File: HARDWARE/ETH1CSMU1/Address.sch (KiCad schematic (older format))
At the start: 16 parts, among them U1501 STEF4S

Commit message: check in
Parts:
- C1501, C1502: footprint (none) -> SMD:C_0603_Symbol1
- R1501, R1502, R1503, R1504: footprint (none) -> SMD:R_0603_Symbol10
- U1501: footprint (none) -> Housings_DFN_QFN:DFN-10-1EP_3x3mm_Pitch0.5mm
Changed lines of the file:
@@
 F 0 "R1501" V 5843 3250 50  0000 C CNN
 F 1 "100" V 5934 3250 50  0000 C CNN
-F 2 "" V 5980 3250 50  0001 C CNN
+F 2 "SMD:R_0603_Symbol10" V 5980 3250 50  0001 C CNN
 F 3 "~" H 6050 3250 50  0001 C CNN
 	1    6050 3250
@@
 F 0 "R1502" V 5843 4050 50  0000 C CNN
 F 1 "100" V 5934 4050 50  0000 C CNN
-F 2 "" V 5980 4050 50  0001 C CNN
+F 2 "SMD:R_0603_Symbol10" V 5980 4050 50  0001 C CNN
 F 3 "~" H 6050 4050 50  0001 C CNN
 	1    6050 4050
@@
 F 0 "R1503" V 5843 4850 50  0000 C CNN
 F 1 "100" V 5934 4850 50  0000 C CNN
-F 2 "" V 5980 4850 50  0001 C CNN
+F 2 "SMD:R_0603_Symbol10" V 5980 4850 50  0001 C CNN
 F 3 "~" H 6050 4850 50  0001 C CNN
 	1    6050 4850
@@
 F 0 "R1504" V 5843 5650 50  0000 C CNN
 F 1 "100" V 5934 5650 50  0000 C CNN
-F 2 "" V 5980 5650 50  0001 C CNN
+F 2 "SMD:R_0603_Symbol10" V 5980 5650 50  0001 C CNN
 F 3 "~" H 6050 5650 50  0001 C CNN
 	1    6050 5650
@@
 F 0 "U1501" H 5550 2565 50  0000 C CNN
 F 1 "STEF4S" H 5550 2474 50  0000 C CNN
-F 2 "" H 5650 2500 50  0001 C CNN
+F 2 "Housings_DFN_QFN:DFN-10-1EP_3x3mm_Pitch0.5mm" H 5650 2500 50  0001 C CNN
 F 3 "" H 5650 2500 50  0001 C CNN
 	1    5550 2000
@@
 F 0 "C1501" H 4915 2546 50  0000 L CNN
 F 1 "100n" H 4915 2455 50  0000 L CNN
-F 2 "" H 4838 2350 50  0001 C CNN
+F 2 "SMD:C_0603_Symbol1" H 4838 2350 50  0001 C CNN
 F 3 "~" H 4800 2500 50  0001 C CNN
 	1    4800 2500
@@
 F 0 "C1502" H 6365 1946 50  0000 L CNN
 F 1 "100n" H 6365 1855 50  0000 L CNN
-F 2 "" H 6288 1750 50  0001 C CNN
+F 2 "SMD:C_0603_Symbol1" H 6288 1750 50  0001 C CNN
 F 3 "~" H 6250 1900 50  0001 C CNN
 	1    6250 1900

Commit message: Check in
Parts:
- C1503: footprint (none) -> SMD:C_0603_Symbol6
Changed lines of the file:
@@
 F 0 "C1503" H 6815 1946 50  0000 L CNN
 F 1 "1u" H 6815 1855 50  0000 L CNN
-F 2 "" H 6738 1750 50  0001 C CNN
+F 2 "SMD:C_0603_Symbol6" H 6738 1750 50  0001 C CNN
 F 3 "~" H 6700 1900 50  0001 C CNN
 	1    6700 1900

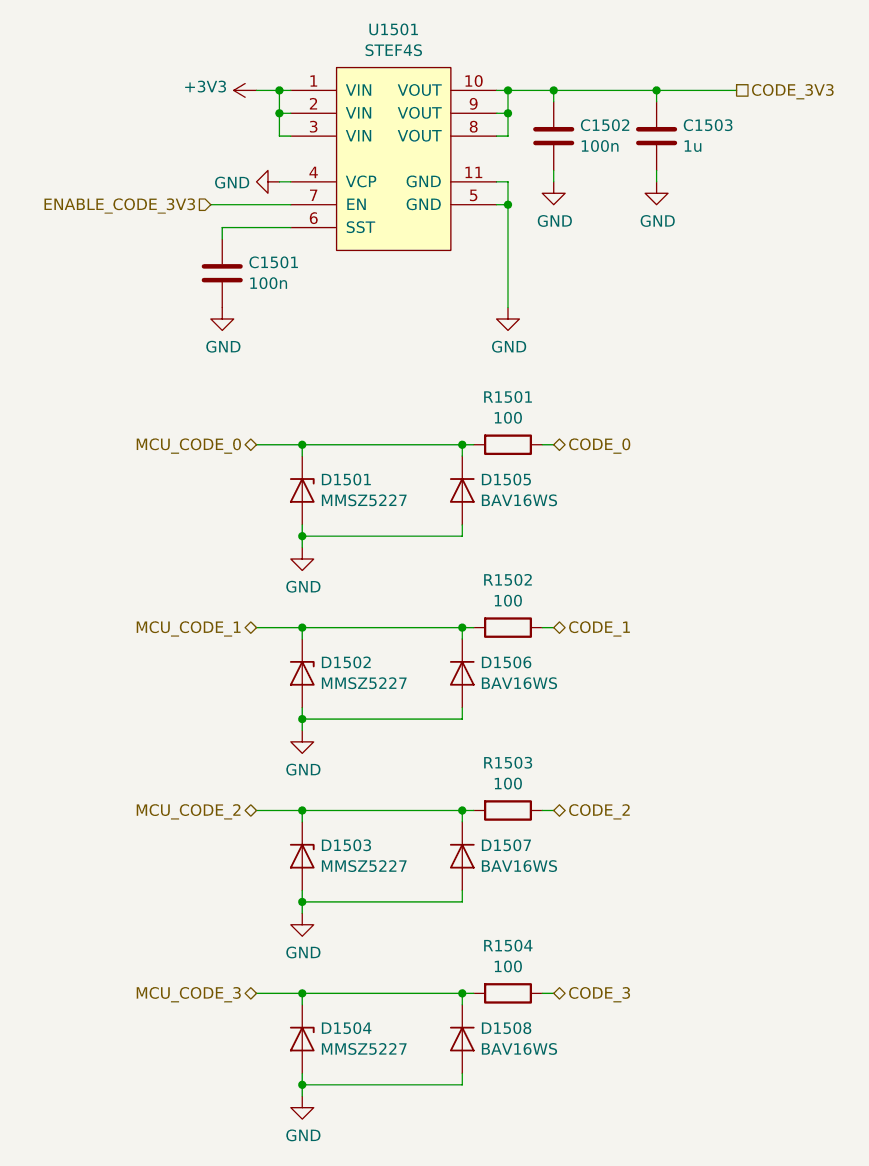
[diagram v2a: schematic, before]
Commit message: Added test circuits, bug fix.
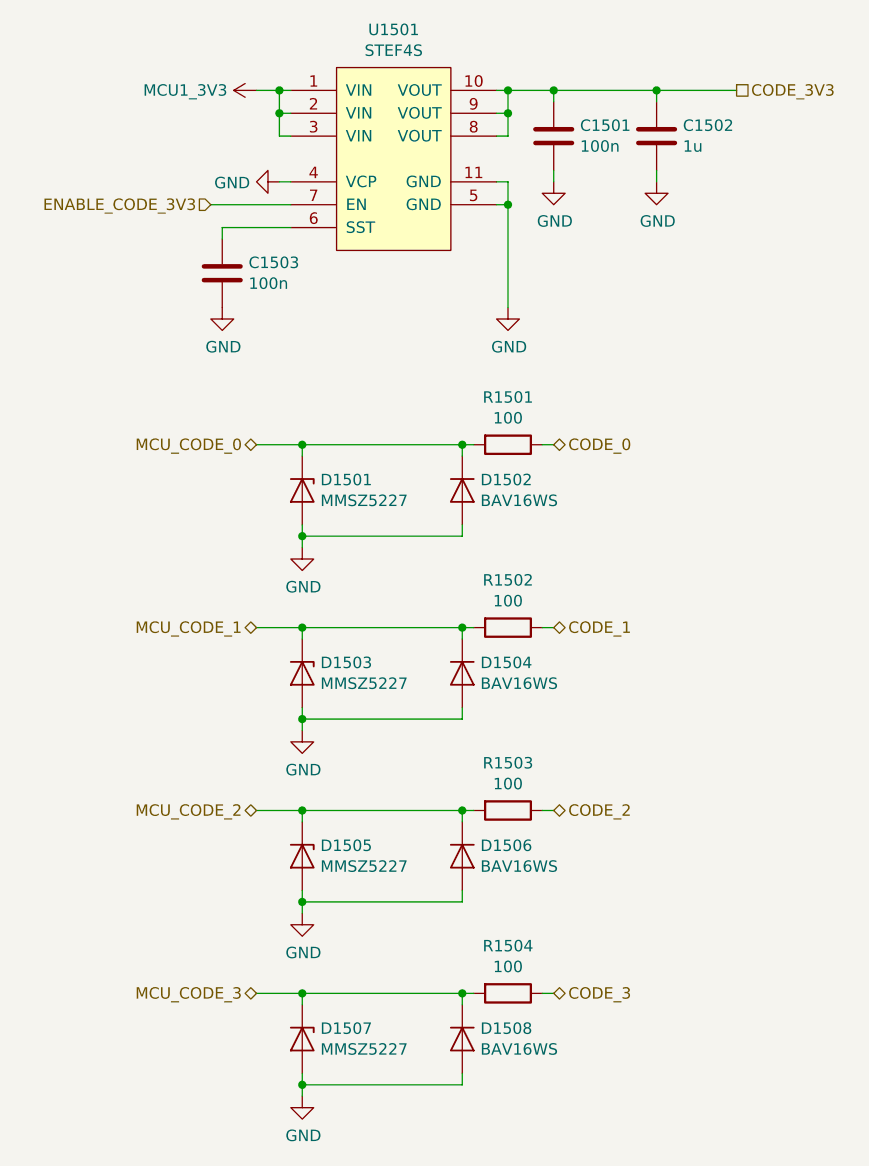
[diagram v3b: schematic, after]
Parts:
- renumbered C1502 to C1501, C1503 to C1502, C1501 to C1503, D1505 to D1502, D1502 to D1503, D1506 to D1504, D1503 to D1505, D1507 to D1506, D1504 to D1507
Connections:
- net +3V3 renamed MCU1_3V3
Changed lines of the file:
@@
 $Descr A4 11693 8268
 encoding utf-8
-Sheet 15 15
+Sheet 15 16
 Title ""
 Date ""
@@
 $EndComp
 $Comp
-L Device:D D1505
+L Device:D D1502
 U 1 1 5C0E460B
 P 5850 3450
-F 0 "D1505" V 5804 3529 50  0000 L CNN
+F 0 "D1502" V 5804 3529 50  0000 L CNN
 F 1 "BAV16WS" V 5895 3529 50  0000 L CNN
 F 2 "Diodes_SMD:D_SOD-323_HandSoldering" H 5850 3450 50  0001 C CNN
@@
 	5850 3650 5850 3600
 $Comp
-L power:GND #PWR01504
+L power:GND #PWR01507
 U 1 1 5C0E4AA9
 P 5150 3700
-F 0 "#PWR01504" H 5150 3450 50  0001 C CNN
+F 0 "#PWR01507" H 5150 3450 50  0001 C CNN
 F 1 "GND" H 5155 3527 50  0000 C CNN
 F 2 "" H 5150 3700 50  0001 C CNN
@@
 CODE_3V3
 $Comp
-L power:+3V3 #PWR01502
-U 1 1 5C0E762F
-P 4950 1700
-F 0 "#PWR01502" H 4950 1550 50  0001 C CNN
-F 1 "+3V3" V 4965 1828 50  0000 L CNN
-F 2 "" H 4950 1700 50  0001 C CNN
-F 3 "" H 4950 1700 50  0001 C CNN
-	1    4950 1700
-	0    -1   -1   0
-$EndComp
-$Comp
-L Device:D D1506
+L Device:D D1504
 U 1 1 5C12B8C6
 P 5850 4250
-F 0 "D1506" V 5804 4329 50  0000 L CNN
+F 0 "D1504" V 5804 4329 50  0000 L CNN
 F 1 "BAV16WS" V 5895 4329 50  0000 L CNN
 F 2 "Diodes_SMD:D_SOD-323_HandSoldering" H 5850 4250 50  0001 C CNN
@@
 	5850 4050 5900 4050
 $Comp
-L Device:D_Zener D1502
+L Device:D_Zener D1503
 U 1 1 5C12B8CF
 P 5150 4250
-F 0 "D1502" V 5104 4329 50  0000 L CNN
+F 0 "D1503" V 5104 4329 50  0000 L CNN
 F 1 "MMSZ5227" V 5195 4329 50  0000 L CNN
 F 2 "Diodes_SMD:D_SOD-123" H 5150 4250 50  0001 C CNN
@@
 	5850 4450 5850 4400
 $Comp
-L power:GND #PWR01505
+L power:GND #PWR01508
 U 1 1 5C12B8DC
 P 5150 4500
-F 0 "#PWR01505" H 5150 4250 50  0001 C CNN
+F 0 "#PWR01508" H 5150 4250 50  0001 C CNN
 F 1 "GND" H 5155 4327 50  0000 C CNN
 F 2 "" H 5150 4500 50  0001 C CNN
@@
 Connection ~ 5150 4050
 $Comp
-L Device:D D1507
+L Device:D D1506
 U 1 1 5C12C933
 P 5850 5050
-F 0 "D1507" V 5804 5129 50  0000 L CNN
+F 0 "D1506" V 5804 5129 50  0000 L CNN
 F 1 "BAV16WS" V 5895 5129 50  0000 L CNN
 F 2 "Diodes_SMD:D_SOD-323_HandSoldering" H 5850 5050 50  0001 C CNN
@@
 	5850 4850 5900 4850
 $Comp
-L Device:D_Zener D1503
+L Device:D_Zener D1505
 U 1 1 5C12C93B
 P 5150 5050
-F 0 "D1503" V 5104 5129 50  0000 L CNN
+F 0 "D1505" V 5104 5129 50  0000 L CNN
 F 1 "MMSZ5227" V 5195 5129 50  0000 L CNN
 F 2 "Diodes_SMD:D_SOD-123" H 5150 5050 50  0001 C CNN
@@
 	5850 5250 5850 5200
 $Comp
-L power:GND #PWR01506
+L power:GND #PWR01509
 U 1 1 5C12C947
 P 5150 5300
-F 0 "#PWR01506" H 5150 5050 50  0001 C CNN
+F 0 "#PWR01509" H 5150 5050 50  0001 C CNN
 F 1 "GND" H 5155 5127 50  0000 C CNN
 F 2 "" H 5150 5300 50  0001 C CNN
@@
 	5850 5650 5900 5650
 $Comp
-L Device:D_Zener D1504
+L Device:D_Zener D1507
 U 1 1 5C12C959
 P 5150 5850
-F 0 "D1504" V 5104 5929 50  0000 L CNN
+F 0 "D1507" V 5104 5929 50  0000 L CNN
 F 1 "MMSZ5227" V 5195 5929 50  0000 L CNN
 F 2 "Diodes_SMD:D_SOD-123" H 5150 5850 50  0001 C CNN
@@
 	5850 6050 5850 6000
 $Comp
-L power:GND #PWR01507
+L power:GND #PWR01510
 U 1 1 5C12C965
 P 5150 6100
-F 0 "#PWR01507" H 5150 5850 50  0001 C CNN
+F 0 "#PWR01510" H 5150 5850 50  0001 C CNN
 F 1 "GND" H 5155 5927 50  0000 C CNN
 F 2 "" H 5150 6100 50  0001 C CNN
@@
 Connection ~ 5050 1700
 $Comp
-L power:GND #PWR01508
+L power:GND #PWR01506
 U 1 1 5C0DDDA0
 P 6050 2650
-F 0 "#PWR01508" H 6050 2400 50  0001 C CNN
+F 0 "#PWR01506" H 6050 2400 50  0001 C CNN
 F 1 "GND" H 6055 2477 50  0000 C CNN
 F 2 "" H 6050 2650 50  0001 C CNN
@@
 	5100 2200 4750 2200
 $Comp
-L power:GND #PWR01503
+L power:GND #PWR01502
 U 1 1 5C0E284A
 P 5050 2100
-F 0 "#PWR01503" H 5050 1850 50  0001 C CNN
+F 0 "#PWR01502" H 5050 1850 50  0001 C CNN
 F 1 "GND" V 5055 1972 50  0000 R CNN
 F 2 "" H 5050 2100 50  0001 C CNN
@@
 	5050 2100 5100 2100
 $Comp
-L Device:C C1501
+L Device:C C1503
 U 1 1 5C0E6BCC
 P 4800 2500
-F 0 "C1501" H 4915 2546 50  0000 L CNN
+F 0 "C1503" H 4915 2546 50  0000 L CNN
 F 1 "100n" H 4915 2455 50  0000 L CNN
 F 2 "SMD:C_0603_Symbol1" H 4838 2350 50  0001 C CNN
@@
 	4800 2300 4800 2350
 $Comp
-L power:GND #PWR01501
+L power:GND #PWR01505
 U 1 1 5C0E8A75
 P 4800 2650
-F 0 "#PWR01501" H 4800 2400 50  0001 C CNN
+F 0 "#PWR01505" H 4800 2400 50  0001 C CNN
 F 1 "GND" H 4805 2477 50  0000 C CNN
 F 2 "" H 4800 2650 50  0001 C CNN
@@
 ENABLE_CODE_3V3
 $Comp
-L Device:C C1502
+L Device:C C1501
 U 1 1 5C0EFAE2
 P 6250 1900
-F 0 "C1502" H 6365 1946 50  0000 L CNN
+F 0 "C1501" H 6365 1946 50  0000 L CNN
 F 1 "100n" H 6365 1855 50  0000 L CNN
 F 2 "SMD:C_0603_Symbol1" H 6288 1750 50  0001 C CNN
@@
 $EndComp
 $Comp
-L Device:C C1503
+L Device:C C1502
 U 1 1 5C0F2F4D
 P 6700 1900
-F 0 "C1503" H 6815 1946 50  0000 L CNN
+F 0 "C1502" H 6815 1946 50  0000 L CNN
 F 1 "1u" H 6815 1855 50  0000 L CNN
 F 2 "SMD:C_0603_Symbol6" H 6738 1750 50  0001 C CNN
@@
 	6700 1700 6250 1700
 $Comp
-L power:GND #PWR01509
+L power:GND #PWR01503
 U 1 1 5C0F750B
 P 6250 2100
-F 0 "#PWR01509" H 6250 1850 50  0001 C CNN
+F 0 "#PWR01503" H 6250 1850 50  0001 C CNN
 F 1 "GND" H 6255 1927 50  0000 C CNN
 F 2 "" H 6250 2100 50  0001 C CNN
@@
 	6250 2100 6250 2050
 $Comp
-L power:GND #PWR01510
+L power:GND #PWR01504
 U 1 1 5C0F8662
 P 6700 2100
-F 0 "#PWR01510" H 6700 1850 50  0001 C CNN
+F 0 "#PWR01504" H 6700 1850 50  0001 C CNN
 F 1 "GND" H 6705 1927 50  0000 C CNN
 F 2 "" H 6700 2100 50  0001 C CNN
@@
 Wire Wire Line
 	6700 2100 6700 2050
+$Comp
+L power_local:MCU1_3V3 #PWR0101
+U 1 1 5C34968B
+P 4950 1700
+F 0 "#PWR0101" H 4950 1600 50  0001 C CNN
+F 1 "MCU1_3V3" V 4950 1827 50  0000 L CNN
+F 2 "" H 4950 1700 50  0000 C CNN
+F 3 "" H 4950 1700 50  0000 C CNN
+	1    4950 1700
+	0    -1   -1   0
+$EndComp
 $EndSCHEMATC
